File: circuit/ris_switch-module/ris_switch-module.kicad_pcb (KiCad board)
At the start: 2 copper layers, 60 x 100 mm, 28 parts, among them J1 JST-PH-5P-M, J2 JST-PH-5P-M, J3 JST-B2PS-VH-M, J4 JST-PH-2P-M, J5 JST-PH-2P-M, J6 JST-PH-2P-M, J7 JST-PH-2P-M, J8 JST-PH-2P-M, J9 JST-PH-2P-M, K1 SRD-03VDC-SL-C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

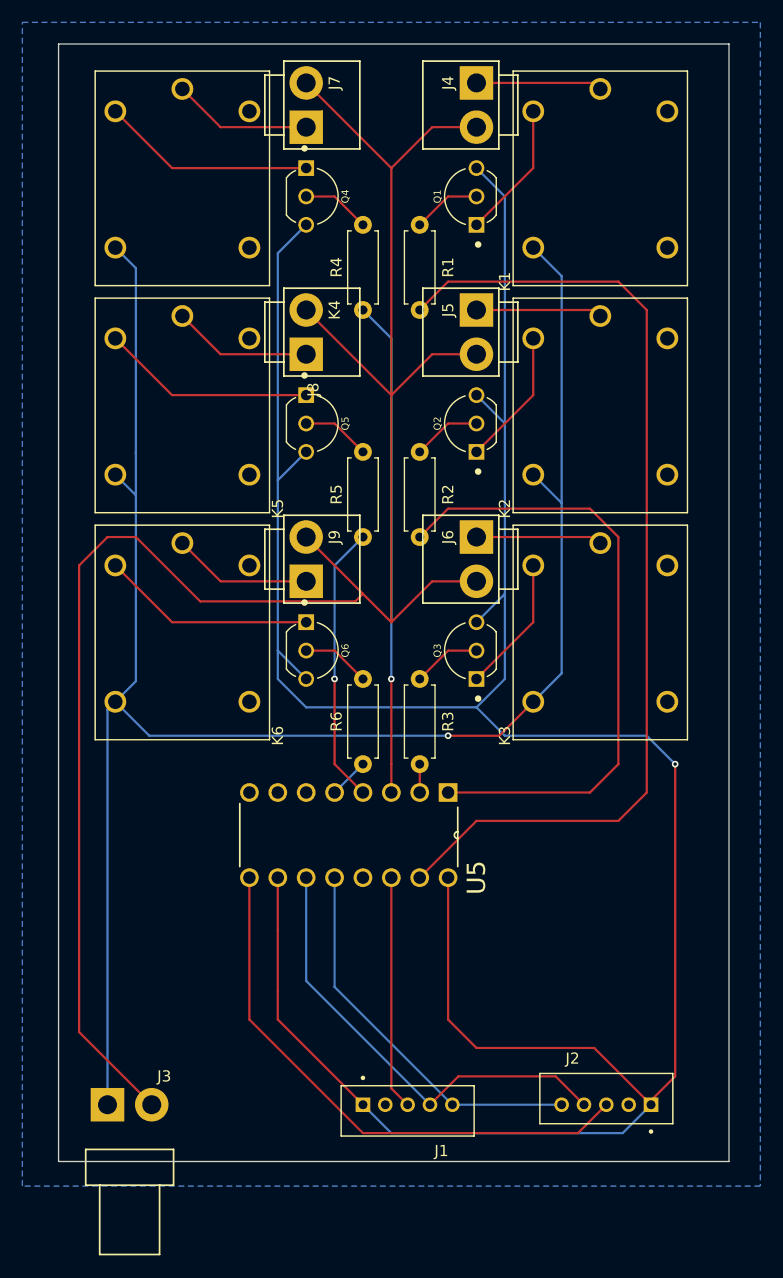
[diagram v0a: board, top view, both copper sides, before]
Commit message: Updated Circuit with Side Outputs & Mosfets
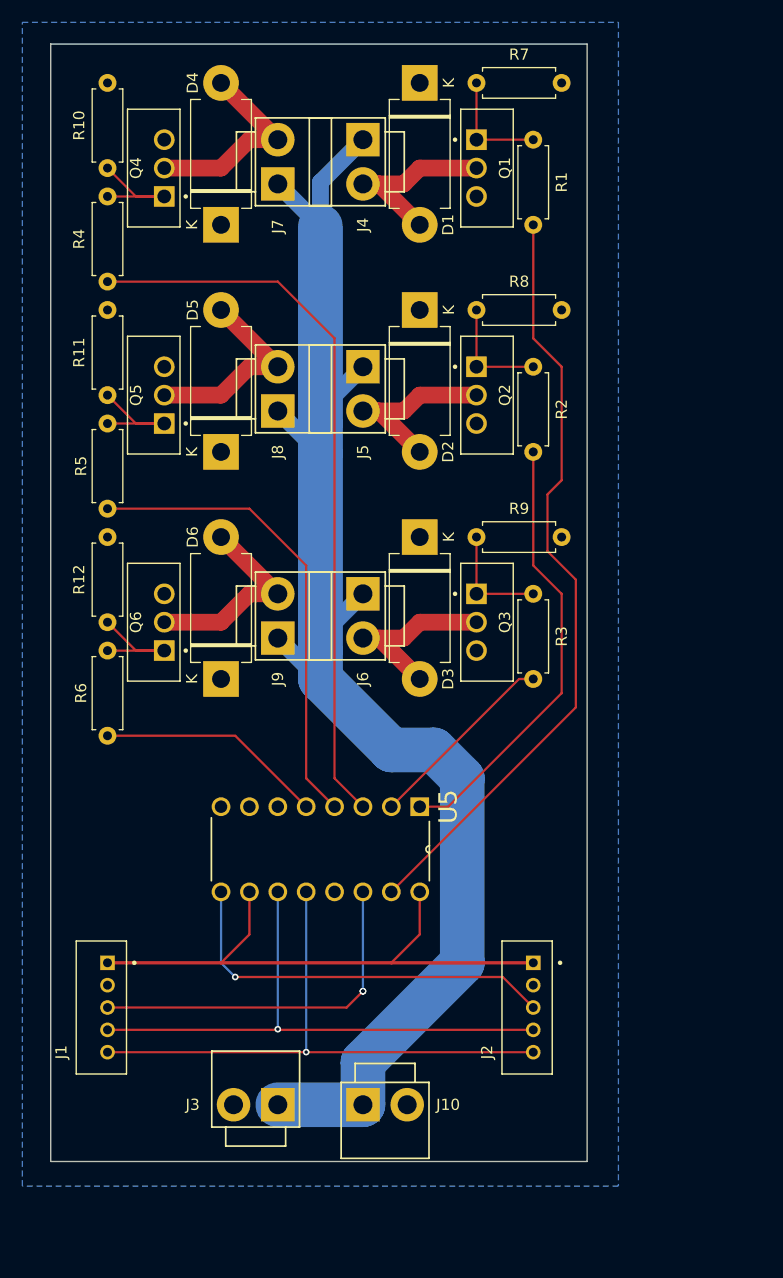
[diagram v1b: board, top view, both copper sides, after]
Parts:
- removed K1, K2, K3, K4, K5, K6: SRD-03VDC-SL-C, SRD-03VDC-SL-C:RELAY_SRD-03VDC-SL-C
- added D1: D, Diode_THT:D_DO-201AD_P12.70mm_Horizontal, F.Cu at (147.3, 58.4)
- added D2: D, Diode_THT:D_DO-201AD_P12.70mm_Horizontal, F.Cu at (147.3, 78.7)
- added D3: D, Diode_THT:D_DO-201AD_P12.70mm_Horizontal, F.Cu at (147.3, 99.1)
- added D4: D, Diode_THT:D_DO-201AD_P12.70mm_Horizontal, F.Cu at (129.5, 71.1)
- added D5: D, Diode_THT:D_DO-201AD_P12.70mm_Horizontal, F.Cu at (129.5, 91.4)
- added D6: D, Diode_THT:D_DO-201AD_P12.70mm_Horizontal, F.Cu at (129.5, 111.8)
- added J10: JST-B2PS-VH-M, JST-B2P-VH:B2P-VH, F.Cu at (144.2, 149.9)
- added R10: R-10k, Resistor_THT:R_Axial_DIN0207_L6.3mm_D2.5mm_P7.62mm_Horizontal, F.Cu at (119.4, 58.4)
- added R11: R-10k, Resistor_THT:R_Axial_DIN0207_L6.3mm_D2.5mm_P7.62mm_Horizontal, F.Cu at (119.4, 78.7)
- added R12: R-10k, Resistor_THT:R_Axial_DIN0207_L6.3mm_D2.5mm_P7.62mm_Horizontal, F.Cu at (119.4, 99.1)
- added R7: R-10k, Resistor_THT:R_Axial_DIN0207_L6.3mm_D2.5mm_P7.62mm_Horizontal, F.Cu at (160.0, 58.4)
- added R8: R-10k, Resistor_THT:R_Axial_DIN0207_L6.3mm_D2.5mm_P7.62mm_Horizontal, F.Cu at (160.0, 78.7)
- added R9: R-10k, Resistor_THT:R_Axial_DIN0207_L6.3mm_D2.5mm_P7.62mm_Horizontal, F.Cu at (160.0, 99.1)
- J3: footprint JST-B2PS-VH:B2PS-VH -> JST-B2P-VH:B2P-VH
- Q1, Q2, Q3, Q4, Q5, Q6: value BC337-40 -> IRLZ44N; footprint 2N3904TF:TO92254P520H877-3 -> MOSFET-IRLZ44N:TO254P1054X469X1930-3
- R1, R2, R3, R4, R5, R6: value R-470 -> R-220
- moved J1 28.9 mm to (118.8, 141.2), turned to 90 degrees
- moved R4 23.0 mm to (119.4, 76.2)
- moved R5 23.0 mm to (119.4, 96.5)
- moved R6 23.0 mm to (119.4, 116.8)
- moved Q5 14.7 mm to (123.5, 86.4), turned to 90 degrees
- moved Q4 14.7 mm to (123.5, 66.0), turned to 90 degrees
- moved Q6 14.7 mm to (123.5, 106.7), turned to 90 degrees
- moved R2 12.7 mm to (157.5, 91.4)
- moved R1 12.7 mm to (157.5, 71.1)
- moved R3 12.7 mm to (157.5, 111.8)
- moved J4 11.4 mm to (142.2, 65.5)
- moved J5 11.4 mm to (142.2, 85.8)
- moved J6 11.4 mm to (142.2, 106.1)
- moved J3 11.3 mm to (132.6, 149.9), turned to 180 degrees
- moved J2 10.8 mm to (156.9, 141.2), turned to 90 degrees
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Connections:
- J1 pad 2: Net-(J1-Pin_2) -> GND
- J2 pad 2: Net-(J1-Pin_2) -> GND
- J3 pad 1: Net-(J3-Pin_1) -> Net-(D1-K)
- J3 pad 2: Net-(J3-Pin_2) -> GND
- J4 pad 1: Net-(J4-Pin_1) -> Net-(D1-K)
- J4 pad 2: Net-(J3-Pin_2) -> Net-(D1-A)
- J5 pad 1: Net-(J5-Pin_1) -> Net-(D1-K)
- J5 pad 2: Net-(J3-Pin_2) -> Net-(D2-A)
- J6 pad 1: Net-(J6-Pin_1) -> Net-(D1-K)
- J6 pad 2: Net-(J3-Pin_2) -> Net-(D3-A)
- J7 pad 1: Net-(J7-Pin_1) -> Net-(D1-K)
- J7 pad 2: Net-(J3-Pin_2) -> Net-(D4-A)
- J8 pad 1: Net-(J8-Pin_1) -> Net-(D1-K)
- J8 pad 2: Net-(J3-Pin_2) -> Net-(D5-A)
- J9 pad 1: Net-(J9-Pin_1) -> Net-(D1-K)
- J9 pad 2: Net-(J3-Pin_2) -> Net-(D6-A)
- Q1 pad 1: Net-(Q1-E) -> Net-(Q1-Pad1)
- Q1 pad 2: Net-(Q1-B) -> Net-(D1-A)
- Q1 pad 3: Net-(J1-Pin_1) -> GND
- Q2 pad 1: Net-(Q2-E) -> Net-(Q2-Pad1)
- Q2 pad 2: Net-(Q2-B) -> Net-(D2-A)
- Q2 pad 3: Net-(J1-Pin_1) -> GND
- Q3 pad 1: Net-(Q3-E) -> Net-(Q3-Pad1)
- Q3 pad 2: Net-(Q3-B) -> Net-(D3-A)
- Q3 pad 3: Net-(J1-Pin_1) -> GND
- Q4 pad 1: Net-(Q4-E) -> Net-(Q4-Pad1)
- Q4 pad 2: Net-(Q4-B) -> Net-(D4-A)
- Q4 pad 3: Net-(J1-Pin_1) -> GND
- Q5 pad 1: Net-(Q5-E) -> Net-(Q5-Pad1)
- Q5 pad 2: Net-(Q5-B) -> Net-(D5-A)
- Q5 pad 3: Net-(J1-Pin_1) -> GND
- Q6 pad 1: Net-(Q6-E) -> Net-(Q6-Pad1)
- Q6 pad 2: Net-(Q6-B) -> Net-(D6-A)
- Q6 pad 3: Net-(J1-Pin_1) -> GND
- R1 pad 2: Net-(Q1-B) -> Net-(Q1-Pad1)
- R2 pad 2: Net-(Q2-B) -> Net-(Q2-Pad1)
- R3 pad 2: Net-(Q3-B) -> Net-(Q3-Pad1)
- R4 pad 2: Net-(Q4-B) -> Net-(Q4-Pad1)
- R5 pad 2: Net-(Q5-B) -> Net-(Q5-Pad1)
- R6 pad 2: Net-(Q6-B) -> Net-(Q6-Pad1)
- U5 pad 13: Net-(J1-Pin_2) -> GND
- U5 pad 8: Net-(J1-Pin_2) -> GND
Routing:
- net Net-(J1-Pin_1): track 261.9 -> 52.9 mm, vias 1 -> 0
- net Net-(J3-Pin_2): track 180.4 -> 0.00 mm
- net Net-(J3-Pin_1): track 167.6 -> 0.00 mm, vias 1 -> 0
- net Net-(D1-K): track 0.00 -> 136.2 mm
- net Net-(U5-Q3): track 44.2 -> 65.4 mm, vias 1 -> 0
- net Net-(U5-Q0): track 89.1 -> 69.2 mm
- net Net-(Q6-E): track 19.2 -> 0.00 mm
- net Net-(Q4-E): track 19.2 -> 0.00 mm
- net Net-(Q5-E): track 19.2 -> 0.00 mm
- net Net-(D6-A): track 0.00 -> 18.4 mm
- net Net-(D5-A): track 0.00 -> 18.4 mm
- net Net-(D4-A): track 0.00 -> 18.4 mm
- net Net-(J1-Pin_5): track 34.5 -> 52.4 mm, vias 0 -> 1
- net Net-(U5-Q4): track 25.0 -> 42.5 mm, vias 1 -> 0
- net Net-(D3-A): track 0.00 -> 17.3 mm
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- added copper zone on B.Cu, net GND
- removed copper zone on B.Cu, net Net-(J1-Pin_2)
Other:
- board size 60 x 100 mm -> 48 x 100 mm

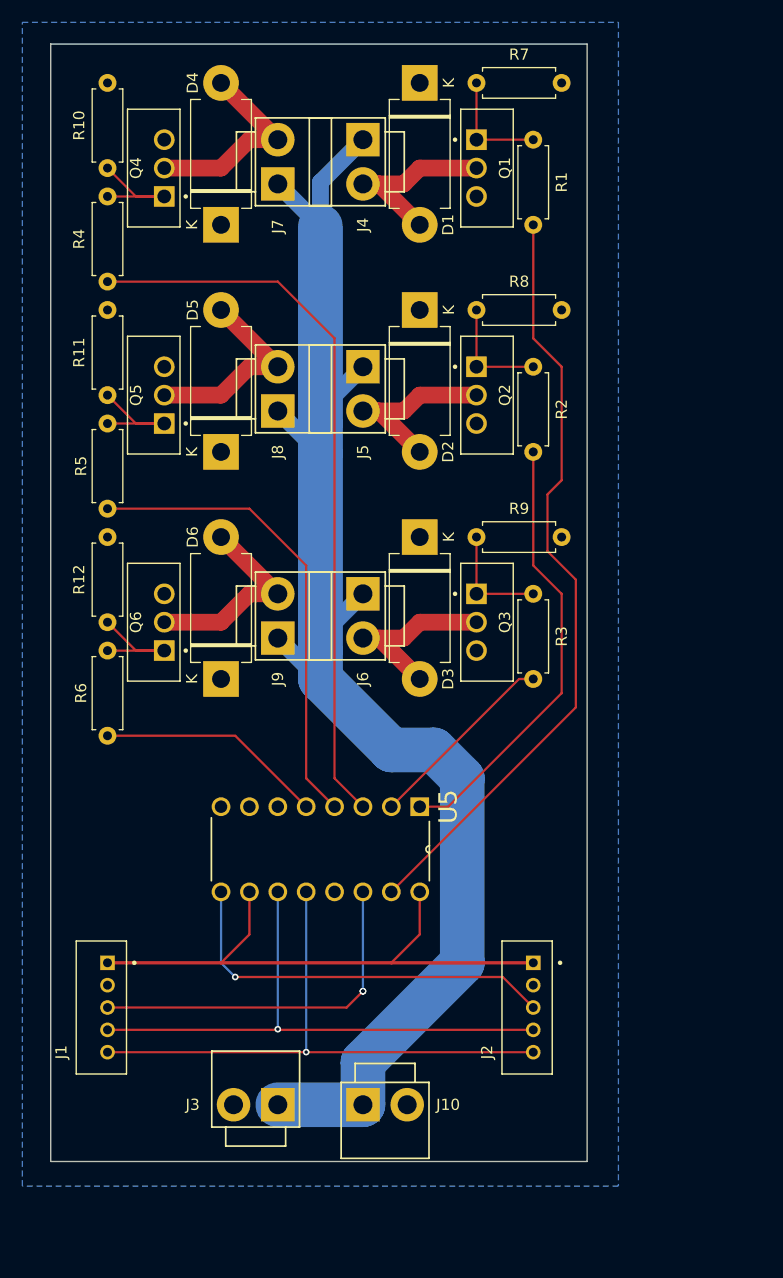
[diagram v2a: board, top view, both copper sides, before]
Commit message: Fixed Circuit by DRC
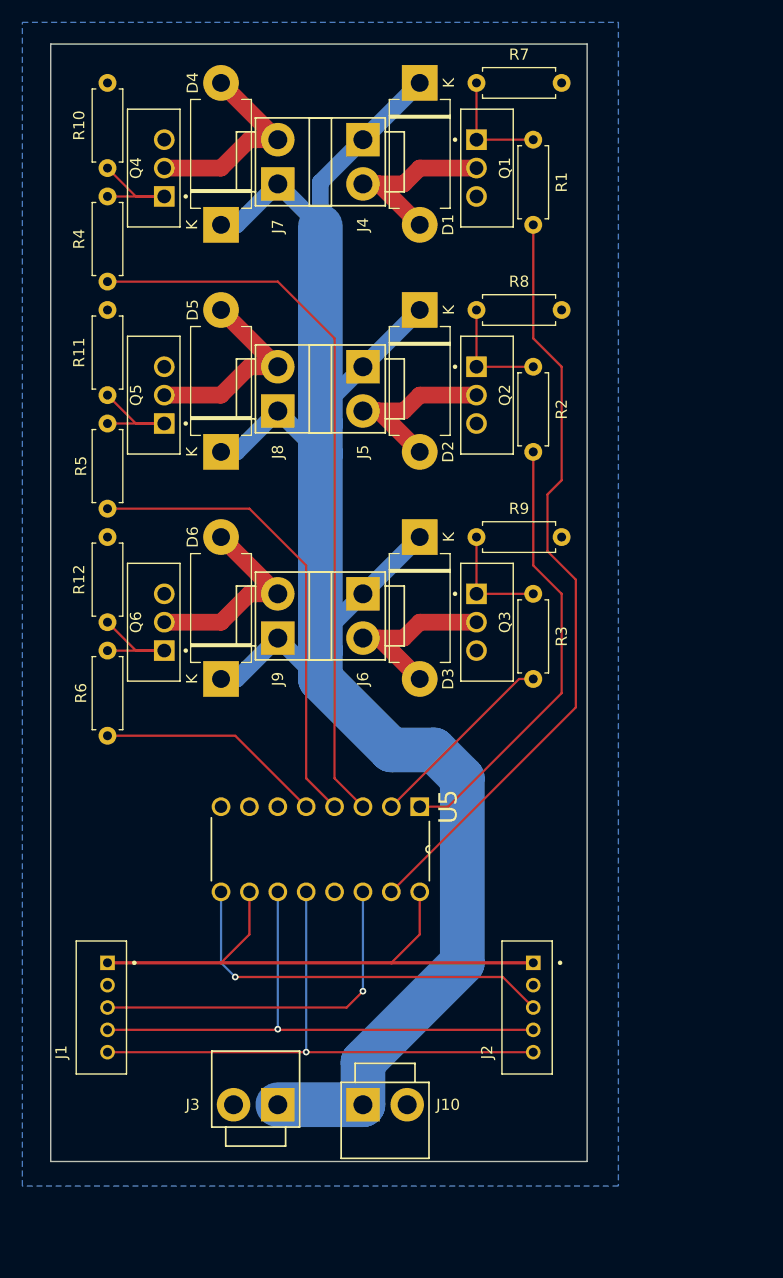
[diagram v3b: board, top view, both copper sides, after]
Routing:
- net Net-(D1-K): track 136.2 -> 177.5 mm
- net Net-(J1-Pin_3): vias 2 -> 1
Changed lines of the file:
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@@
 			(outputformat 1)
 			(mirror no)
-			(drillshape 1)
+			(drillshape 0)
 			(scaleselection 1)
-			(outputdirectory "")
+			(outputdirectory "gerber/")
 		)
 	)
@@
 	(segment
 		(start 140.78 141.16)
-		(end 142.24 139.7)
+		(end 119.38 141.16)
 		(width 0.2)
 		(layer "F.Cu")
@@
 	)
 	(segment
-		(start 119.38 141.16)
+		(start 142.24 139.7)
 		(end 140.78 141.16)
 		(width 0.2)
@@
 		(net 12)
 	)
-	(via
-		(at 142.24 139.7)
-		(size 0.6)
-		(drill 0.3)
-		(layers "F.Cu" "B.Cu")
-		(net 12)
-	)
 	(segment
 		(start 142.24 139.7)
@@
 	)
 	(segment
-		(start 134.62 108.1)
-		(end 138.28 111.76)
-		(width 1.5)
-		(layer "B.Cu")
-		(net 14)
-	)
-	(segment
 		(start 138.43 67.31)
 		(end 138.43 71.27)
@@
 	)
 	(segment
+		(start 129.54 91.44)
+		(end 130.96 91.44)
+		(width 1.5)
+		(layer "B.Cu")
+		(net 14)
+	)
+	(segment
 		(start 142.24 146.05)
 		(end 151.13 137.16)
@@
 	)
 	(segment
+		(start 130.96 91.44)
+		(end 134.62 87.78)
+		(width 1.5)
+		(layer "B.Cu")
+		(net 14)
+	)
+	(segment
 		(start 138.43 88.9)
 		(end 138.43 71.27)
@@
 	)
 	(segment
+		(start 138.28 111.76)
+		(end 138.43 111.76)
+		(width 0.2)
+		(layer "B.Cu")
+		(net 14)
+	)
+	(segment
+		(start 129.54 71.12)
+		(end 130.96 71.12)
+		(width 1.5)
+		(layer "B.Cu")
+		(net 14)
+	)
+	(segment
+		(start 147.32 99.06)
+		(end 142.24 104.14)
+		(width 1.5)
+		(layer "B.Cu")
+		(net 14)
+	)
+	(segment
 		(start 142.24 104.14)
 		(end 138.43 107.95)
@@
 	)
 	(segment
-		(start 138.28 111.76)
-		(end 138.43 111.76)
-		(width 0.2)
+		(start 134.62 108.1)
+		(end 138.28 111.76)
+		(width 1.5)
+		(layer "B.Cu")
+		(net 14)
+	)
+	(segment
+		(start 147.32 78.74)
+		(end 142.24 83.82)
+		(width 1.5)
 		(layer "B.Cu")
 		(net 14)
@@
 	)
 	(segment
+		(start 130.96 111.76)
+		(end 134.62 108.1)
+		(width 1.5)
+		(layer "B.Cu")
+		(net 14)
+	)
+	(segment
+		(start 129.54 111.76)
+		(end 130.96 111.76)
+		(width 1.5)
+		(layer "B.Cu")
+		(net 14)
+	)
+	(segment
 		(start 151.13 137.16)
 		(end 151.13 120.65)
@@
 		(layer "B.Cu")
 		(net 14)
+	)
+	(segment
+		(start 147.32 58.42)
+		(end 142.24 63.5)
+		(width 1.5)
+		(layer "B.Cu")
+		(net 14)
+	)
+	(segment
+		(start 130.96 71.12)
+		(end 134.62 67.46)
+		(width 1.5)
+		(layer "B.Cu")
+		(net 14)

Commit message: Exported Circuits to Gerber files
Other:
- board text added: "RIS - SWITCH MODULE v1.0.0 - SAM DIXON"
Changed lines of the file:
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@@
 			(drillshape 0)
 			(scaleselection 1)
-			(outputdirectory "gerber/")
+			(outputdirectory "ris_switch-module_gerber/")
 		)
 	)
@@
 		(at 129.54 130.81 -90)
 		(property "Reference" "U5"
-			(at -7.62 -20.32 90)
+			(at 0 -20.32 90)
 			(layer "F.SilkS")
 			(effects
 				(font
-					(size 1.640874 1.640874)
+					(size 1 1)
 					(thickness 0.15)
 				)
@@
 			(layer "F.Fab")
 		)
-		(fp_text user "K"
-			(at 0 -2.6 90)
-			(layer "F.SilkS")
-			(effects
-				(font
-					(size 1 1)
-					(thickness 0.15)
-				)
-			)
-		)
 		(fp_text user "${REFERENCE}"
 			(at 7.62 0 90)
@@
 		(at 118.83 141.16 90)
 		(property "Reference" "J1"
-			(at -4 -3.585 90)
+			(at -4 3.725 90)
 			(layer "F.SilkS")
 			(effects
@@
 			(layer "F.Fab")
 		)
-		(fp_text user "K"
-			(at 0 -2.6 90)
-			(layer "F.SilkS")
-			(effects
-				(font
-					(size 1 1)
-					(thickness 0.15)
-				)
-			)
-		)
 		(fp_text user "${REFERENCE}"
 			(at 7.62 0 90)
@@
 			(layer "F.Fab")
 		)
-		(fp_text user "K"
-			(at 0 -2.6 90)
-			(layer "F.SilkS")
-			(effects
-				(font
-					(size 1 1)
-					(thickness 0.15)
-				)
-			)
-		)
 		(fp_text user "${REFERENCE}"
 			(at 7.62 0 90)
@@
 		(fp_text user "K"
 			(at 0 -2.6 90)
-			(layer "F.SilkS")
-			(effects
-				(font
-					(size 1 1)
-					(thickness 0.15)
-				)
-			)
-		)
-		(fp_text user "K"
-			(at 0 -2.6 90)
 			(layer "F.Fab")
 			(effects
@@
 		(fp_text user "K"
 			(at 0 -2.6 90)
-			(layer "F.SilkS")
-			(effects
-				(font
-					(size 1 1)
-					(thickness 0.15)
-				)
-			)
-		)
-		(fp_text user "K"
-			(at 0 -2.6 90)
 			(layer "F.Fab")
 			(effects
@@
 		(layer "Edge.Cuts")
 	)
+	(gr_text "RIS - SWITCH MODULE\nv1.0.0 - SAM DIXON"
+		(at 158.115 134.62 90)
+		(layer "F.SilkS")
+		(effects
+			(font
+				(size 1 1)
+				(thickness 0.15)
+			)
+			(justify left bottom)
+		)
+	)
 	(segment
